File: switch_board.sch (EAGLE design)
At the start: 15 parts, among them U1 ADG904BRUZ, U2 ADP3330ARTZ-2.5-R7

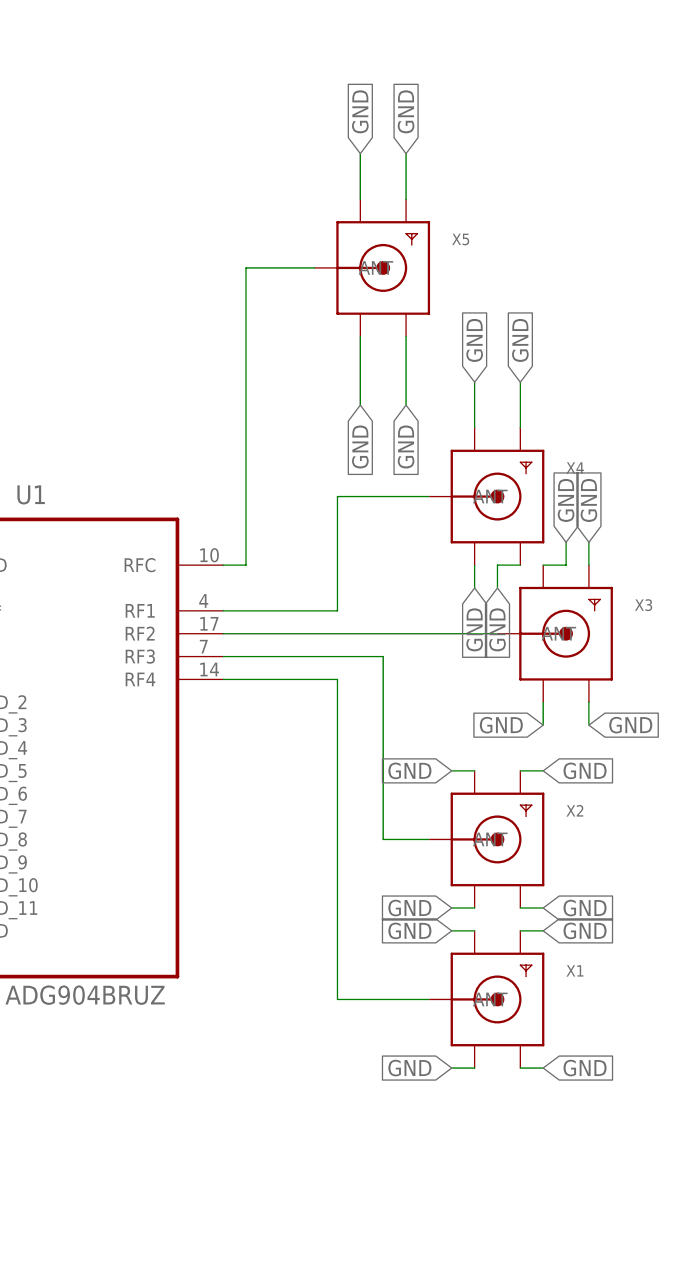
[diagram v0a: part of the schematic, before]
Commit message: Add DC Blocking Caps
Added 100uf caps for dc blocking on rf lines. Also updated readme
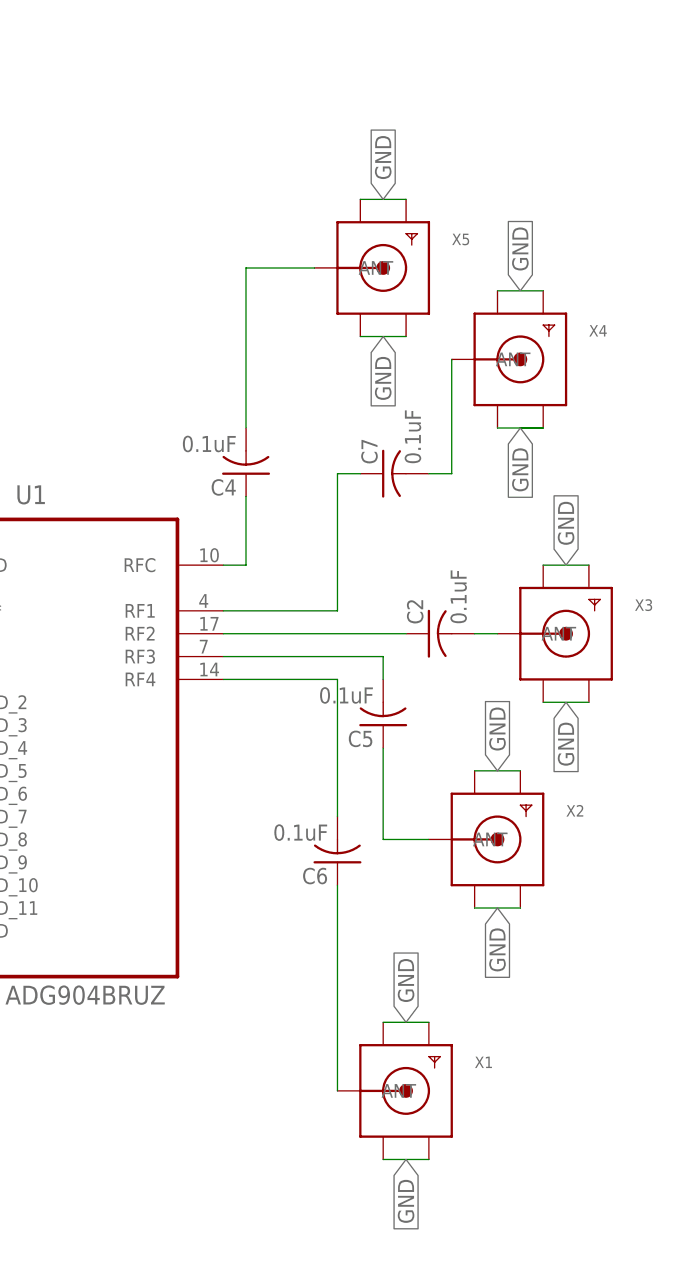
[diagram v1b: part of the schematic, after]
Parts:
- added C2, C4, C5, C6, C7: 0.1uF, resistor:C-USC0603
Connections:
- removed net RF2: U1.RF2, X3.ANT
- new net N$3: C5.1, X2.ANT
- new net N$4: C4.1, U1.RFC
- new net N$5: C2.1, U1.RF2
- new net N$7: C2.2, X3.ANT
- new net N$8: C7.2, X4.ANT
- new net N$9: C6.1, X1.ANT
- net RF1: now also C7.1; no longer X4.ANT
- net RF3: now also C5.2; no longer X2.ANT
- net RF4: now also C6.2; no longer X1.ANT
- net RFC: now also C4.2; no longer U1.RFC
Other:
- moved on the sheet: X1, X4
